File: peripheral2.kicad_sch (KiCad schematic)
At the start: 55 parts, among them J23 3V3, J24 GND, J25 5V, J27 PJ-320D, J28 screw_term, J29 screw_term, J30 RS485, J32 AUDIO, U12 SN74LVC1G14DBV, U13 SN74LVC1G14DBV, U14 MAX485E, U16 LMV358IDR

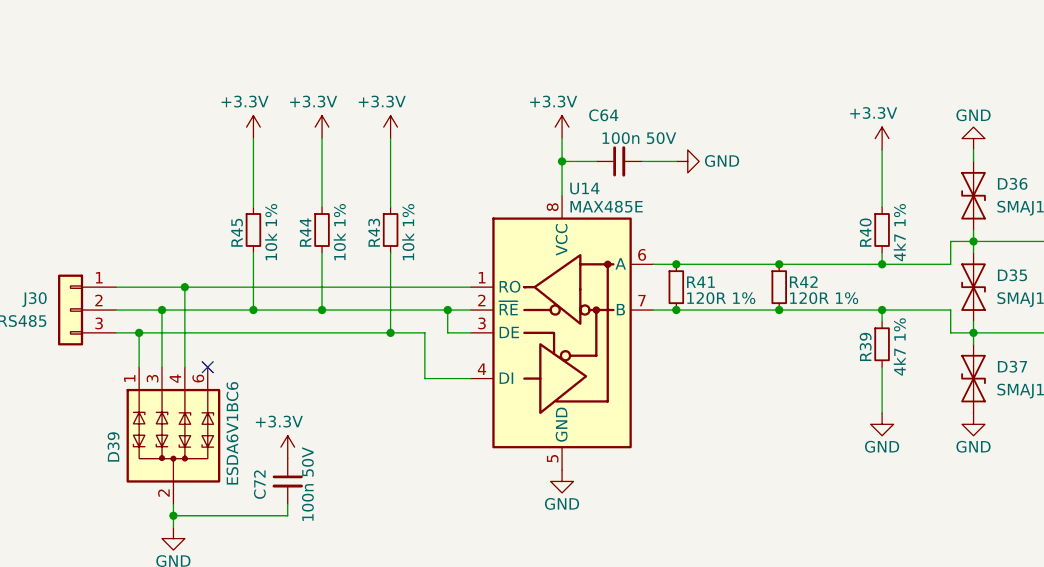
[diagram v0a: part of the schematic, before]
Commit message: kju fix and PCB size increase
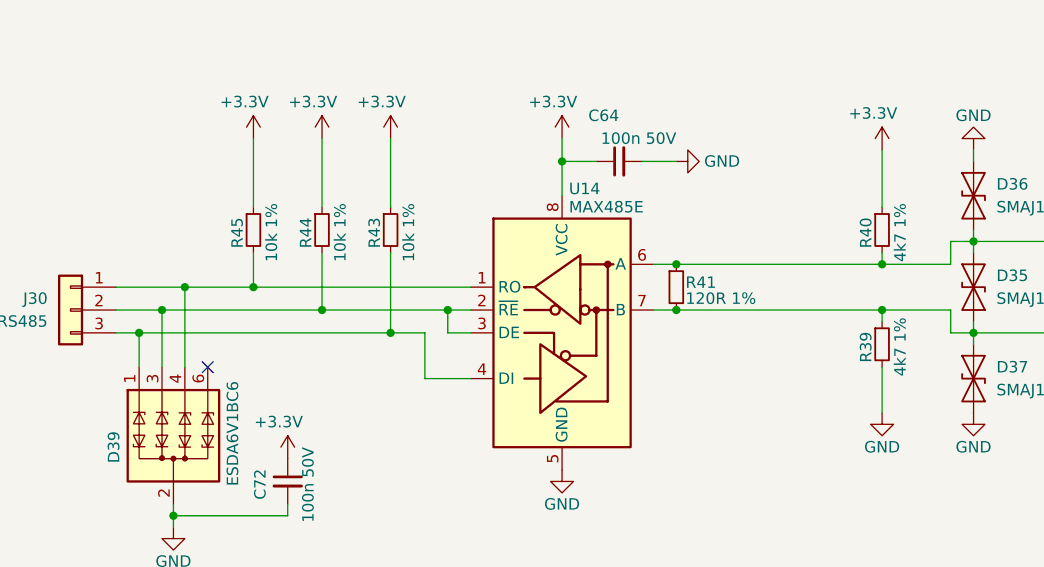
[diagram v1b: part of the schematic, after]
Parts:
- removed R42: 120R 1%, Resistor_SMD:R_0603_1608Metric_Pad0.98x0.95mm_HandSolder, symbol Device:R_Small
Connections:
- net at D39.4 (TVS3), J30.1 (Pin_1), U14.1 (RO): now also R45.2
- net at D39.3 (TVS2), J30.2 (Pin_2), R44.2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: no longer R45.2
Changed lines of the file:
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@@
 	)
 	(junction
-		(at 106.68 160.02)
-		(diameter 0)
-		(color 0 0 0 0)
-	)
-	(junction
 		(at 118.11 160.02)
 		(diameter 0)
@@
 	)
 	(junction
-		(at 106.68 165.1)
-		(diameter 0)
-		(color 0 0 0 0)
-	)
-	(junction
-		(at 48.26 165.1)
-		(diameter 0)
-		(color 0 0 0 0)
-	)
-	(junction
 		(at 260.35 148.59)
 		(diameter 0)
@@
 	)
 	(junction
+		(at 48.26 162.56)
+		(diameter 0)
+		(color 0 0 0 0)
+	)
+	(junction
 		(at 275.59 146.05)
 		(diameter 0)
@@
 	(wire
 		(pts
-			(xy 95.25 160.02) (xy 106.68 160.02)
+			(xy 95.25 160.02) (xy 118.11 160.02)
 		)
 		(stroke
@@
 	(wire
 		(pts
-			(xy 106.68 160.02) (xy 118.11 160.02)
-		)
-		(stroke
-			(width 0)
-			(type default)
-		)
-	)
-	(wire
-		(pts
 			(xy 189.23 54.61) (xy 194.31 54.61)
 		)
@@
 	(wire
 		(pts
-			(xy 48.26 165.1) (xy 55.88 165.1)
+			(xy 38.1 165.1) (xy 55.88 165.1)
 		)
 		(stroke
@@
 	(wire
 		(pts
-			(xy 95.25 165.1) (xy 106.68 165.1)
+			(xy 95.25 165.1) (xy 118.11 165.1)
 		)
 		(stroke
@@
 	(wire
 		(pts
-			(xy 38.1 165.1) (xy 48.26 165.1)
+			(xy 118.11 165.1) (xy 118.11 166.37)
 		)
 		(stroke
@@
 	(wire
 		(pts
-			(xy 118.11 165.1) (xy 118.11 166.37)
+			(xy 189.23 52.07) (xy 189.23 54.61)
 		)
 		(stroke
@@
 	(wire
 		(pts
-			(xy 189.23 52.07) (xy 189.23 54.61)
+			(xy 39.37 187.96) (xy 39.37 189.23)
 		)
 		(stroke
@@
 	(wire
 		(pts
-			(xy 39.37 187.96) (xy 39.37 189.23)
+			(xy 139.7 106.68) (xy 132.08 106.68)
 		)
 		(stroke
@@
 	(wire
 		(pts
-			(xy 139.7 106.68) (xy 132.08 106.68)
+			(xy 48.26 162.56) (xy 72.39 162.56)
 		)
 		(stroke
@@
 	(wire
 		(pts
+			(xy 48.26 158.75) (xy 48.26 162.56)
+		)
+		(stroke
+			(width 0)
+			(type default)
+		)
+	)
+	(wire
+		(pts
 			(xy 240.03 151.13) (xy 240.03 154.94)
 		)
@@
 	(wire
 		(pts
-			(xy 48.26 158.75) (xy 48.26 165.1)
-		)
-		(stroke
-			(width 0)
-			(type default)
-		)
-	)
-	(wire
-		(pts
 			(xy 189.23 57.15) (xy 170.18 57.15)
 		)
@@
 	(wire
 		(pts
-			(xy 40.64 162.56) (xy 72.39 162.56)
+			(xy 40.64 162.56) (xy 48.26 162.56)
 		)
 		(stroke
@@
 	(wire
 		(pts
-			(xy 106.68 165.1) (xy 118.11 165.1)
-		)
-		(stroke
-			(width 0)
-			(type default)
-		)
-	)
-	(wire
-		(pts
 			(xy 104.14 97.79) (xy 92.71 97.79)
 		)
@@
 					(unit 1)
 				)
-			)
-		)
-	)
-	(symbol
-		(lib_id "Device:R_Small")
-		(at 106.68 162.56 0)
-		(unit 1)
-		(exclude_from_sim no)
-		(in_bom yes)
-		(on_board yes)
-		(dnp no)
-		(property "Reference" "R42"
-			(at 107.696 162.052 0)
-			(effects
-				(font
-					(size 1.27 1.27)
-				)
-				(justify left)
-			)
-		)
-		(property "Value" "120R 1%"
-			(at 107.696 163.83 0)
-			(effects
-				(font
-					(size 1.27 1.27)
-				)
-				(justify left)
-			)
-		)
-		(property "Footprint" "Resistor_SMD:R_0603_1608Metric_Pad0.98x0.95mm_HandSolder"
-			(at 106.68 162.56 0)
-			(effects
-				(font
-					(size 1.27 1.27)
-				)
-				(hide yes)
-			)
-		)
-		(property "Datasheet" "~"
-			(at 106.68 162.56 0)
-			(effects
-				(font
-					(size 1.27 1.27)
-				)
-				(hide yes)
-			)
-		)
-		(property "Description" ""
-			(at 106.68 162.56 0)
-			(effects
-				(font
-					(size 1.27 1.27)
-				)
-				(hide yes)
-			)
-		)
-		(property "jlc" ""
-			(at 106.68 162.56 90)
-			(effects
-				(font
-					(size 1.27 1.27)
-				)
-				(hide yes)
-			)
-		)
-		(pin "1"
-		)
-		(pin "2"
-		)
-		(instances
-			(project "beam_kit_1"
-				(path "/3a707576-1044-44db-8cf8-deb84fe605c8/f99848e2-c114-48ca-84d4-6dd921defc9c"
-					(reference "R42")
-					(unit 1)
-				)

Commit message: layout
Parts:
- added D40, D41: LED R, LED_SMD:LED_0603_1608Metric_Pad1.05x0.95mm_HandSolder, symbol Device:LED_Small
- added R42, R54: 10k 1%, Resistor_SMD:R_0603_1608Metric_Pad0.98x0.95mm_HandSolder, symbol Device:R_Small
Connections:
- net +3V3: now also R54.2
- net CH_RIGHT: now also D38.1 (TVS1); no longer D38.3 (TVS2)
- net GND: now also D40.1 (K), D41.1 (K)
- net VBUS: now also R42.2
- net at J32.3 (Pin_3), R53.1: now also D38.3 (TVS2); no longer D38.1 (TVS1)
- new net: D40.2 (A), R42.1
- new net: D41.2 (A), R54.1

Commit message: layout done
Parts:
- J28, J29: jlc C474952 -> C395734
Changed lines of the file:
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@@
 			)
 		)
-		(property "jlc" "C474952"
+		(property "jlc" "C395734"
 			(at 151.13 161.29 0)
 			(effects
@@
 			)
 		)
-		(property "jlc" "C474952"
+		(property "jlc" "C395734"
 			(at 163.83 161.29 0)
 			(effects

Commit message: codes and fixes
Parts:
- added D42, D43: LED R, LED_SMD:LED_0603_1608Metric_Pad1.05x0.95mm_HandSolder, symbol Device:LED_Small
- added J26: TERM, Connector_PinHeader_2.54mm:PinHeader_1x02_P2.54mm_Vertical, symbol Connector_Generic:Conn_01x02
- added R55, R56: 5k1 1%, Resistor_SMD:R_0603_1608Metric_Pad0.98x0.95mm_HandSolder, symbol Device:R_Small
- C60, C61, C62, C64, C65, C69: footprint Capacitor_SMD:C_0603_1608Metric -> Capacitor_SMD:C_0603_1608Metric_Pad1.08x0.95mm_HandSolder; jlc (none) -> C14663
- C67, C68: footprint Capacitor_SMD:C_0603_1608Metric -> Capacitor_SMD:C_0603_1608Metric_Pad1.08x0.95mm_HandSolder
- C70: footprint Capacitor_SMD:C_0603_1608Metric -> Capacitor_SMD:C_0603_1608Metric_Pad1.08x0.95mm_HandSolder; jlc (none) -> C1588
- C71, C72: jlc (none) -> C14663
- D40, D41: jlc (none) -> C2286
- J24: jlc (none) -> C492423
- J30, J32: jlc (none) -> C49257
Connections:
- net +3.3V: now also R55.2, R56.2
- net B: now also J26.2 (Pin_2); no longer R41.2
- net at D39.4 (TVS3), J30.1 (Pin_1), R45.2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: now also D43.1 (K)
- net at D39.3 (TVS2), J30.2 (Pin_2), R44.2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: now also D42.1 (K)
- new net: J26.1 (Pin_1), R41.2
- new net: D42.2 (A), R55.1
- new net: D43.2 (A), R56.1
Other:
- moved on the sheet: D35, D36, D37, J28, J29, J30, R39, R40, R43, R44, R45

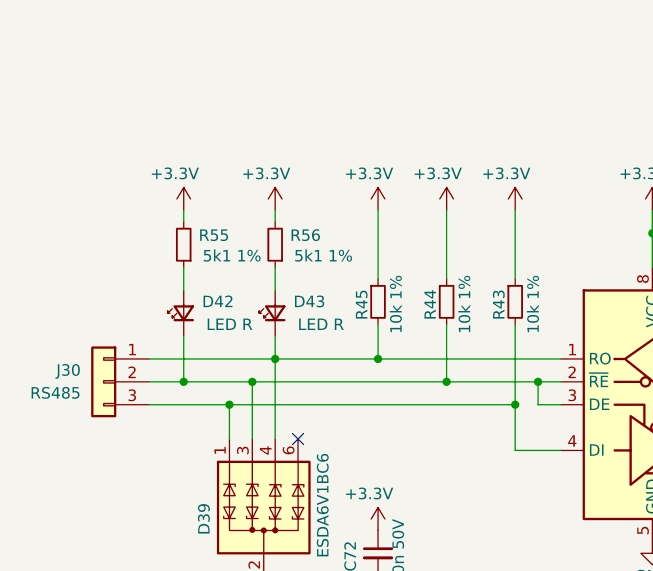
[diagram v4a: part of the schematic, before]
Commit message: RS leds fix
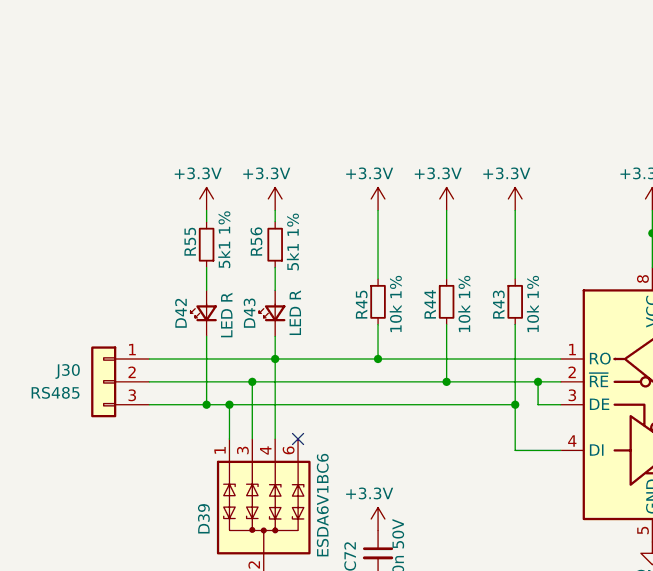
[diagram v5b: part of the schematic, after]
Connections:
- net at D39.1 (TVS1), J30.3 (Pin_3), R43.2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: now also D42.1 (K)
- net at D39.3 (TVS2), J30.2 (Pin_2), R44.2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: no longer D42.1 (K)
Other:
- moved on the sheet: D42, R55
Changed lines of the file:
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@@
 	)
 	(junction
-		(at 30.48 165.1)
-		(diameter 0)
-		(color 0 0 0 0)
-	)
-	(junction
 		(at 269.24 43.18)
 		(diameter 0)
@@
 	)
 	(junction
+		(at 33.02 167.64)
+		(diameter 0)
+		(color 0 0 0 0)
+	)
+	(junction
 		(at 38.1 165.1)
 		(diameter 0)
@@
 	(wire
 		(pts
-			(xy 26.67 165.1) (xy 30.48 165.1)
-		)
-		(stroke
-			(width 0)
-			(type default)
-		)
-	)
-	(wire
-		(pts
 			(xy 222.25 148.59) (xy 222.25 151.13)
 		)
@@
 	(wire
 		(pts
-			(xy 26.67 167.64) (xy 35.56 167.64)
+			(xy 26.67 167.64) (xy 33.02 167.64)
 		)
 		(stroke
@@
 	(wire
 		(pts
+			(xy 33.02 160.02) (xy 33.02 167.64)
+		)
+		(stroke
+			(width 0)
+			(type default)
+		)
+	)
+	(wire
+		(pts
 			(xy 109.22 97.79) (xy 119.38 97.79)
 		)
@@
 	(wire
 		(pts
-			(xy 30.48 146.05) (xy 30.48 147.32)
+			(xy 33.02 146.05) (xy 33.02 147.32)
 		)
 		(stroke
@@
 	(wire
 		(pts
-			(xy 30.48 160.02) (xy 30.48 165.1)
+			(xy 39.37 186.69) (xy 39.37 187.96)
 		)
 		(stroke
@@
 	(wire
 		(pts
-			(xy 39.37 186.69) (xy 39.37 187.96)
+			(xy 275.59 146.05) (xy 275.59 148.59)
 		)
 		(stroke
@@
 	(wire
 		(pts
-			(xy 275.59 146.05) (xy 275.59 148.59)
+			(xy 33.02 167.64) (xy 35.56 167.64)
 		)
 		(stroke
@@
 	(wire
 		(pts
-			(xy 30.48 152.4) (xy 30.48 154.94)
+			(xy 33.02 152.4) (xy 33.02 154.94)
 		)
 		(stroke
@@
 	(wire
 		(pts
-			(xy 30.48 165.1) (xy 38.1 165.1)
+			(xy 26.67 165.1) (xy 38.1 165.1)
 		)
 		(stroke
@@
 	(symbol
 		(lib_id "Device:R_Small")
-		(at 30.48 149.86 180)
+		(at 33.02 149.86 180)
 		(unit 1)
 		(exclude_from_sim no)
@@
 		(dnp no)
 		(property "Reference" "R55"
-			(at 35.56 148.844 0)
+			(at 31.242 147.828 90)
 			(effects
 				(font
@@
 		)
 		(property "Value" "5k1 1%"
-			(at 39.116 151.13 0)
+			(at 35.052 146.05 90)
 			(effects
 				(font
@@
 		)
 		(property "Footprint" "Resistor_SMD:R_0603_1608Metric_Pad0.98x0.95mm_HandSolder"
-			(at 30.48 149.86 0)
+			(at 33.02 149.86 0)
 			(effects
 				(font
@@
 		)
 		(property "Datasheet" "~"
-			(at 30.48 149.86 0)
+			(at 33.02 149.86 0)
 			(effects
 				(font
@@
 		)
 		(property "Description" ""
-			(at 30.48 149.86 0)
+			(at 33.02 149.86 0)
 			(effects
 				(font
@@
 		(dnp no)
 		(property "Reference" "D43"
-			(at 44.45 156.21 90)
+			(at 37.846 157.48 0)
 			(effects
 				(font
@@
 		)
 		(property "Value" "LED R"
-			(at 45.72 158.75 90)
+			(at 42.926 157.48 0)
 			(effects
 				(font
@@
 	(symbol
 		(lib_id "Device:LED_Small")
-		(at 30.48 157.48 90)
+		(at 33.02 157.48 90)
 		(unit 1)
 		(exclude_from_sim no)
@@
 		(dnp no)
 		(property "Reference" "D42"
-			(at 34.29 156.21 90)
+			(at 30.226 157.48 0)
 			(effects
 				(font
@@
 		)
 		(property "Value" "LED R"
-			(at 35.56 158.75 90)
+			(at 35.306 157.734 0)
 			(effects
 				(font
@@
 		)
 		(property "Footprint" "LED_SMD:LED_0603_1608Metric_Pad1.05x0.95mm_HandSolder"
-			(at 30.48 157.48 90)
+			(at 33.02 157.48 90)
 			(effects
 				(font
@@
 		)
 		(property "Datasheet" "~"
-			(at 30.48 157.48 90)
+			(at 33.02 157.48 90)
 			(effects
 				(font
@@
 		)
 		(property "Description" ""
-			(at 30.48 157.48 0)
+			(at 33.02 157.48 0)
 			(effects
 				(font
@@
 		)
 		(property "LED" "C2286"
-			(at 30.48 157.48 90)
+			(at 33.02 157.48 90)
 			(effects
 				(font
@@
 		)
 		(property "jlc" "C2286"
-			(at 30.48 157.48 0)
+			(at 33.02 157.48 0)
 			(effects
 				(font
@@
 		(dnp no)
 		(property "Reference" "R56"
-			(at 45.72 148.844 0)
+			(at 38.608 147.828 90)
 			(effects
 				(font
@@
 		)
 		(property "Value" "5k1 1%"
-			(at 49.276 151.13 0)
+			(at 42.672 146.304 90)
 			(effects
 				(font
@@
 	(symbol
 		(lib_id "power:+3.3V")
-		(at 30.48 146.05 0)
+		(at 33.02 146.05 0)
 		(unit 1)
 		(exclude_from_sim no)
@@
 		(dnp no)
 		(property "Reference" "#PWR0235"
-			(at 30.48 149.86 0)
+			(at 33.02 149.86 0)
 			(effects
 				(font
@@
 		)
 		(property "Value" "+3.3V"
-			(at 29.464 141.986 0)
+			(at 32.004 141.986 0)
 			(effects
 				(font
@@
 		)
 		(property "Footprint" ""
-			(at 30.48 146.05 0)
+			(at 33.02 146.05 0)
 			(effects
 				(font
@@
 		)
 		(property "Datasheet" ""
-			(at 30.48 146.05 0)
+			(at 33.02 146.05 0)
 			(effects
 				(font
@@
 		)
 		(property "Description" "Power symbol creates a global label with name \"+3.3V\""
-			(at 30.48 146.05 0)
+			(at 33.02 146.05 0)
 			(effects
 				(font

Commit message: jlc codes filled
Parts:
- R31, R37: jlc (none) -> C22962
- R32, R33, R53: jlc (none) -> C22775
- R39, R40: jlc (none) -> C23162
- R41: jlc (none) -> C22787
- R42, R43, R44, R45, R46, R47, R49, R50, R51, R52, R54: jlc (none) -> C25804
- R48: jlc (none) -> C4190
- R55, R56: jlc (none) -> C23186
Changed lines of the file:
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@@
 			)
 		)
+		(property "jlc" "C4190"
+			(at 201.93 99.06 0)
+			(effects
+				(font
+					(size 1.27 1.27)
+				)
+				(hide yes)
+			)
+		)
 		(pin "1"
 		)
@@
 			)
 		)
-		(property "jlc" ""
+		(property "jlc" "C25804"
 			(at 176.53 104.14 90)
 			(effects
@@
 			)
 		)
-		(property "jlc" ""
+		(property "jlc" "C25804"
 			(at 231.14 125.73 90)
 			(effects
@@
 			)
 		)
+		(property "jlc" "C23186"
+			(at 33.02 149.86 0)
+			(effects
+				(font
+					(size 1.27 1.27)
+				)
+				(hide yes)
+			)
+		)
 		(pin "1"
 		)
@@
 			)
 		)
+		(property "jlc" "C22775"
+			(at 154.94 63.5 0)
+			(effects
+				(font
+					(size 1.27 1.27)
+				)
+				(hide yes)
+			)
+		)
 		(pin "1"
 		)
@@
 			)
 		)
-		(property "jlc" ""
+		(property "jlc" "C25804"
 			(at 106.68 97.79 90)
 			(effects
@@
 			)
 		)
-		(property "jlc" ""
+		(property "jlc" "C25804"
 			(at 129.54 106.68 90)
 			(effects
@@
 			)
 		)
-		(property "jlc" ""
+		(property "jlc" "C23162"
 			(at 123.19 156.21 90)
 			(effects
@@
 			)
 		)
+		(property "jlc" "C22962"
+			(at 133.35 35.56 0)
+			(effects
+				(font
+					(size 1.27 1.27)
+				)
+				(hide yes)
+			)
+		)
 		(pin "1"
 		)
@@
 			)
 		)
-		(property "jlc" ""
+		(property "jlc" "C25804"
 			(at 165.1 93.98 90)
 			(effects
@@
 			)
 		)
-		(property "jlc" ""
+		(property "jlc" "C25804"
 			(at 67.31 156.21 90)
 			(effects
@@
 			)
 		)
-		(property "jlc" ""
+		(property "jlc" "C23162"
 			(at 123.19 168.91 90)
 			(effects
@@
 			)
 		)
+		(property "jlc" "C22775"
+			(at 154.94 41.91 0)
+			(effects
+				(font
+					(size 1.27 1.27)
+				)
+				(hide yes)
+			)
+		)
 		(pin "1"
 		)
@@
 			)
 		)
-		(property "jlc" ""
+		(property "jlc" "C25804"
 			(at 172.72 119.38 90)
 			(effects
@@
 			)
 		)
-		(property "jlc" ""
+		(property "jlc" "C25804"
 			(at 172.72 127 90)
 			(effects
@@
 			)
 		)
-		(property "jlc" ""
+		(property "jlc" "C22787"
 			(at 101.6 162.56 90)
 			(effects
@@
 			)
 		)
-		(property "jlc" ""
+		(property "jlc" "C25804"
 			(at 59.69 156.21 90)
 			(effects
@@
 			)
 		)
-		(property "jlc" ""
+		(property "jlc" "C25804"
 			(at 266.7 125.73 90)
 			(effects
@@
 			)
 		)
+		(property "jlc" "C22775"
+			(at 86.36 109.22 0)
+			(effects
+				(font
+					(size 1.27 1.27)
+				)
+				(hide yes)
+			)
+		)
 		(pin "1"
 		)
@@
 			)
 		)
-		(property "jlc" ""
+		(property "jlc" "C25804"
 			(at 52.07 156.21 90)
 			(effects
@@
 			)
 		)
+		(property "jlc" "C23186"
+			(at 40.64 149.86 0)
+			(effects
+				(font
+					(size 1.27 1.27)
+				)
+				(hide yes)
+			)
+		)
 		(pin "1"
 		)
@@
 			(at 133.35 57.15 0)
 			(effects
+				(font
+					(size 1.27 1.27)
+				)
+				(hide yes)
+			)
+		)
+		(property "jlc" "C22962"
+			(at 133.35 57.15 0)
+			(effects

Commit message: layout done
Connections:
- net +3V3 is gone; now on net +3.3V: J23.1 (Pin_1), J23.2 (Pin_2), J23.3 (Pin_3), J23.4 (Pin_4), J23.5 (Pin_5), J23.6 (Pin_6), R54.2
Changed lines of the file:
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@@
 	)
 	(symbol
+		(lib_id "power:+3.3V")
+		(at 222.25 124.46 0)
+		(unit 1)
+		(exclude_from_sim no)
+		(in_bom yes)
+		(on_board yes)
+		(dnp no)
+		(property "Reference" "#PWR0199"
+			(at 222.25 128.27 0)
+			(effects
+				(font
+					(size 1.27 1.27)
+				)
+				(hide yes)
+			)
+		)
+		(property "Value" "+3.3V"
+			(at 222.25 120.65 0)
+			(effects
+				(font
+					(size 1.27 1.27)
+				)
+			)
+		)
+		(property "Footprint" ""
+			(at 222.25 124.46 0)
+			(effects
+				(font
+					(size 1.27 1.27)
+				)
+				(hide yes)
+			)
+		)
+		(property "Datasheet" ""
+			(at 222.25 124.46 0)
+			(effects
+				(font
+					(size 1.27 1.27)
+				)
+				(hide yes)
+			)
+		)
+		(property "Description" "Power symbol creates a global label with name \"+3.3V\""
+			(at 222.25 124.46 0)
+			(effects
+				(font
+					(size 1.27 1.27)
+				)
+				(hide yes)
+			)
+		)
+		(pin "1"
+		)
+		(instances
+			(project "beam_kit_1"
+				(path "/3a707576-1044-44db-8cf8-deb84fe605c8/f99848e2-c114-48ca-84d4-6dd921defc9c"
+					(reference "#PWR0199")
+					(unit 1)
+				)
+			)
+		)
+	)
+	(symbol
 		(lib_id "Device:C_Small")
 		(at 106.68 90.17 90)
@@
 					(unit 1)
 				)
-			)
-		)
-	)
-	(symbol
-		(lib_id "power:+3.3V")
-		(at 222.25 124.46 0)
-		(unit 1)
-		(exclude_from_sim no)
-		(in_bom yes)
-		(on_board yes)
-		(dnp no)
-		(property "Reference" "#PWR0199"
-			(at 222.25 128.27 0)
-			(effects
-				(font
-					(size 1.27 1.27)
-				)
-				(hide yes)
-			)
-		)
-		(property "Value" "+3V3"
-			(at 222.25 120.65 0)
-			(effects
-				(font
-					(size 1.27 1.27)
-				)
-			)
-		)
-		(property "Footprint" ""
-			(at 222.25 124.46 0)
-			(effects
-				(font
-					(size 1.27 1.27)
-				)
-				(hide yes)
-			)
-		)
-		(property "Datasheet" ""
-			(at 222.25 124.46 0)
-			(effects
-				(font
-					(size 1.27 1.27)
-				)
-				(hide yes)
-			)
-		)
-		(property "Description" ""
-			(at 222.25 124.46 0)
-			(effects
-				(font
-					(size 1.27 1.27)
-				)
-				(hide yes)
-			)
-		)
-		(pin "1"
-		)
-		(instances
-			(project "beam_kit_1"
-				(path "/3a707576-1044-44db-8cf8-deb84fe605c8/f99848e2-c114-48ca-84d4-6dd921defc9c"
-					(reference "#PWR0199")
-					(unit 1)
-				)

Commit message: final version
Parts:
- C60, C61, C62, C64, C65, C69, C71, C72: JLC (none) -> C14663
- C63, C66: JLC (none) -> C16780
- C67: JLC (none) -> C19702
- C70: JLC (none) -> C1588
- D35, D36, D37: JLC (none) -> C908818
- D38, D39: JLC (none) -> C495220
- D40, D41, D42, D43: JLC (none) -> C2286
- J23, J25: JLC (none) -> C37208
- J24: JLC (none) -> C492423
- J26: JLC (none) -> C492401
- J27: JLC (none) -> C431535
- J28, J29: JLC (none) -> C395734
- J30, J32: JLC (none) -> C49257
- MK1: JLC (none) -> C234023
- R31, R37: JLC (none) -> C22962
- R32, R33, R53: JLC (none) -> C22775
- R34, R35: JLC (none) -> C4177
- R39, R40: JLC (none) -> C23162
- R41: JLC (none) -> C22787
- R42, R43, R44, R45, R46, R47, R49, R50, R51, R52, R54: JLC (none) -> C25804
- R48: JLC (none) -> C4190
- R55, R56: JLC (none) -> C23186
- RV1: JLC (none) -> C116316
- U12, U13: JLC (none) -> C7835
- U14: JLC (none) -> C19738
- U16: JLC (none) -> C63813
